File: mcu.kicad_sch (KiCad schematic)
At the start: 42 parts, among them J2 USB-C, J3 UART0, J4 I2C / Qwiic, J5 SPI, J6 WS2812, J7 Spare IO, J8 Rail break-out, Q4 AO3401A, Q5 MMBT3906, SW1 RESET, SW2 BOOT, U5 ESP32-S3-WROOM-1-N16R8, U6 TLV431A, U7 USBLC6-2SC6, U8 USBLC6-2SC6, U9 74AHCT1G125

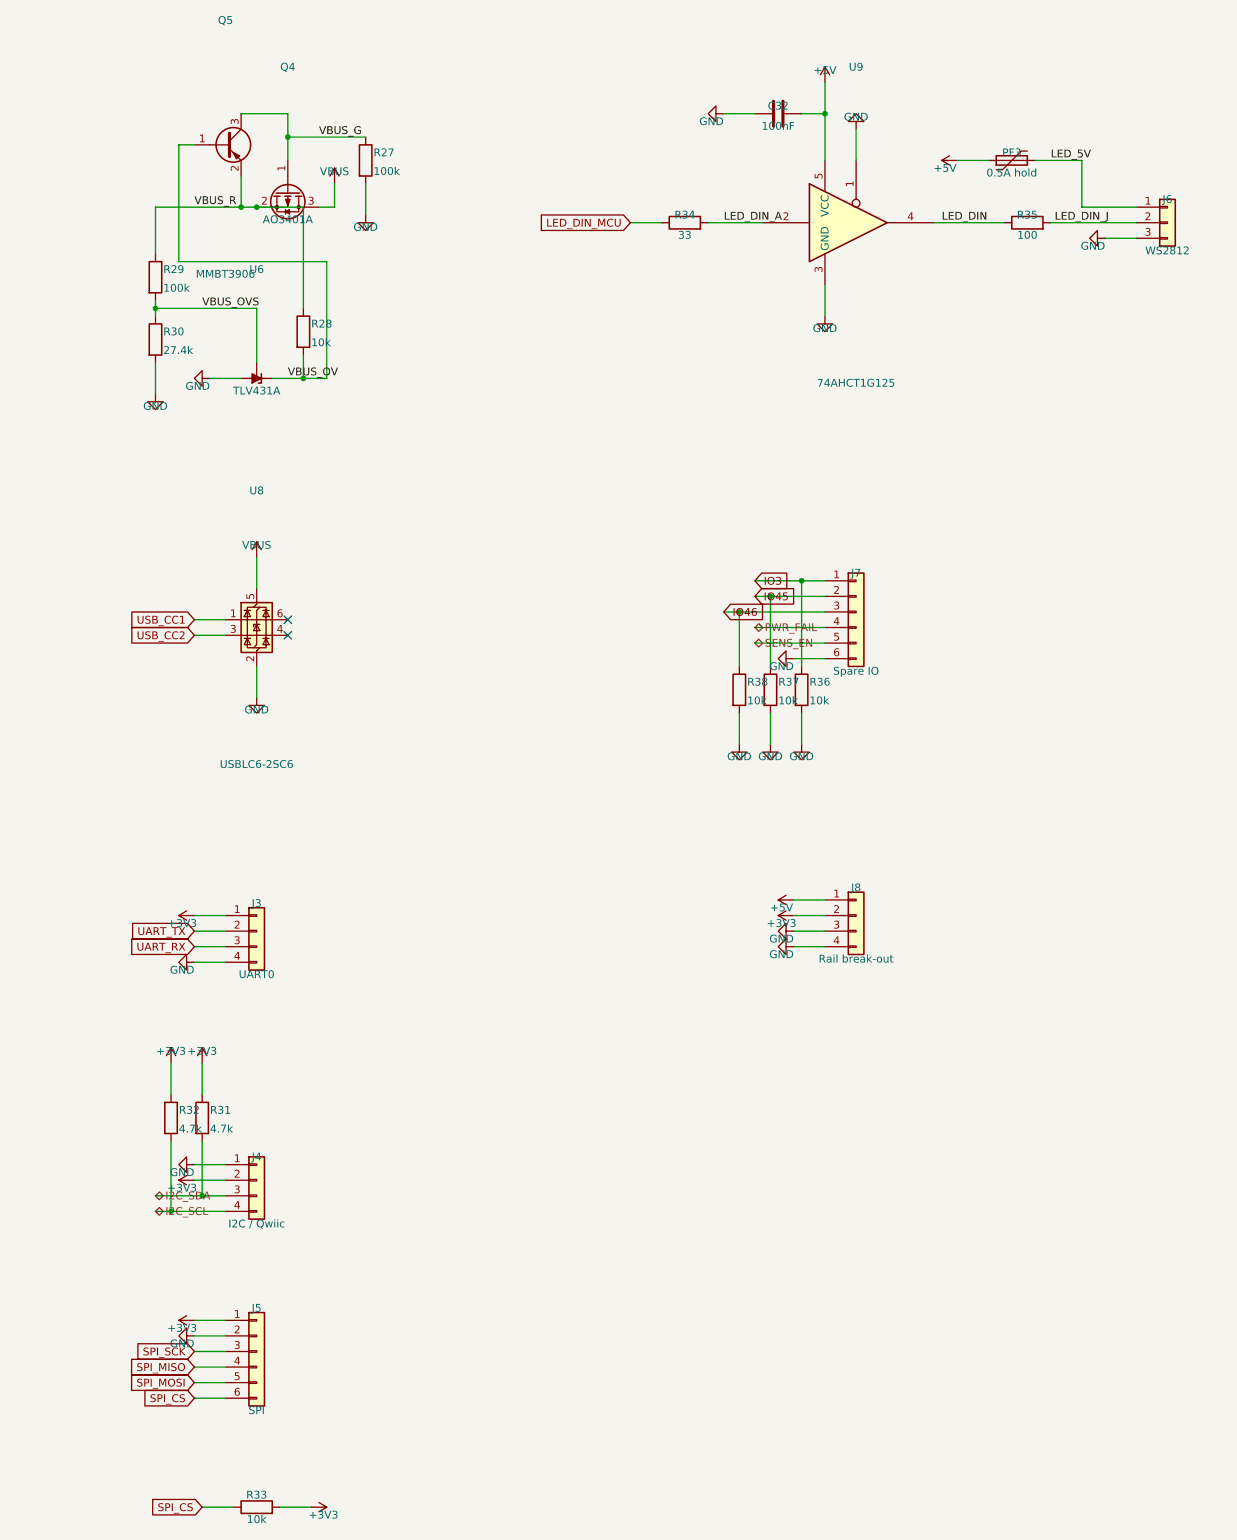
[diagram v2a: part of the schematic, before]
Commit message: Studies 9-11, post-route extraction, strap audit, readable labels, production BOM numbers
New tests, run against the final board:
- audit_routes.py: Dijkstra IR drop over the routed copper (worst 55 mV
  at rated current), SD/USB/CAN routed lengths (USB pair matched to
  1.1 mm), buck switch-node copper area. All clean.
- audit_straps.py: every ESP32-S3 strapping pin against what the netlist
  hangs on it; all five boot in their required state.
- simulate.py 9, stability: the LM5164 ripple-injection criterion across
  the input window. Found the ramp thin (10.6 mV) at a legitimate 8 V
  operating point -- ramp caps changed 3.3 nF -> 2.2 nF, now 15.8 mV+
  everywhere above crank voltages. Board rebuilt: 0 DRC, 0 unconnected,
  0 overlaps.
- simulate.py 10, CAN bus: TJA1051 through the choke and split
  termination into 5 m of terminated line -- 2.00 V dominant at the far
  end, no overshoot.
- simulate.py 11, budgets: enclosure thermal for the in-dash mount
  (sealed ABS is fine in the dash, would exceed the electrolytics' 105 C
  in an engine bay -- documented), fuse derating 69 %, I2C rise time vs
  Qwiic chains, WS2812 count, SD switch drop, connector contacts.
- tolerance MC gains the ride-through corner: 36 ms at caps -20 % /
  load +40 %, still covering a healthy-card flush.

Schematic readability, second pass: net-name labels moved onto short
vertical spurs clear of the circuits (deleting them outright renames
nets to Net-(R5-Pad2) and breaks name-based verification -- now in
gen/README.md), end-labels extend away from what they feed, and the
sensor-switch block redrawn at 1.5x pitch. Reversed-5V behaviour per
connector documented in the README.

BOM production pass: verified LCSC numbers added for the TVS families,
BAT54S, MM3Z zener and 2N7002s (21 numbered lines); the 39 blank lines
are JLC-auto-matched basic R/C; the 12 extended lines that must be
hand-matched in the order UI are listed in README 11. No guessed part
numbers.

gen/README.md gains the readab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
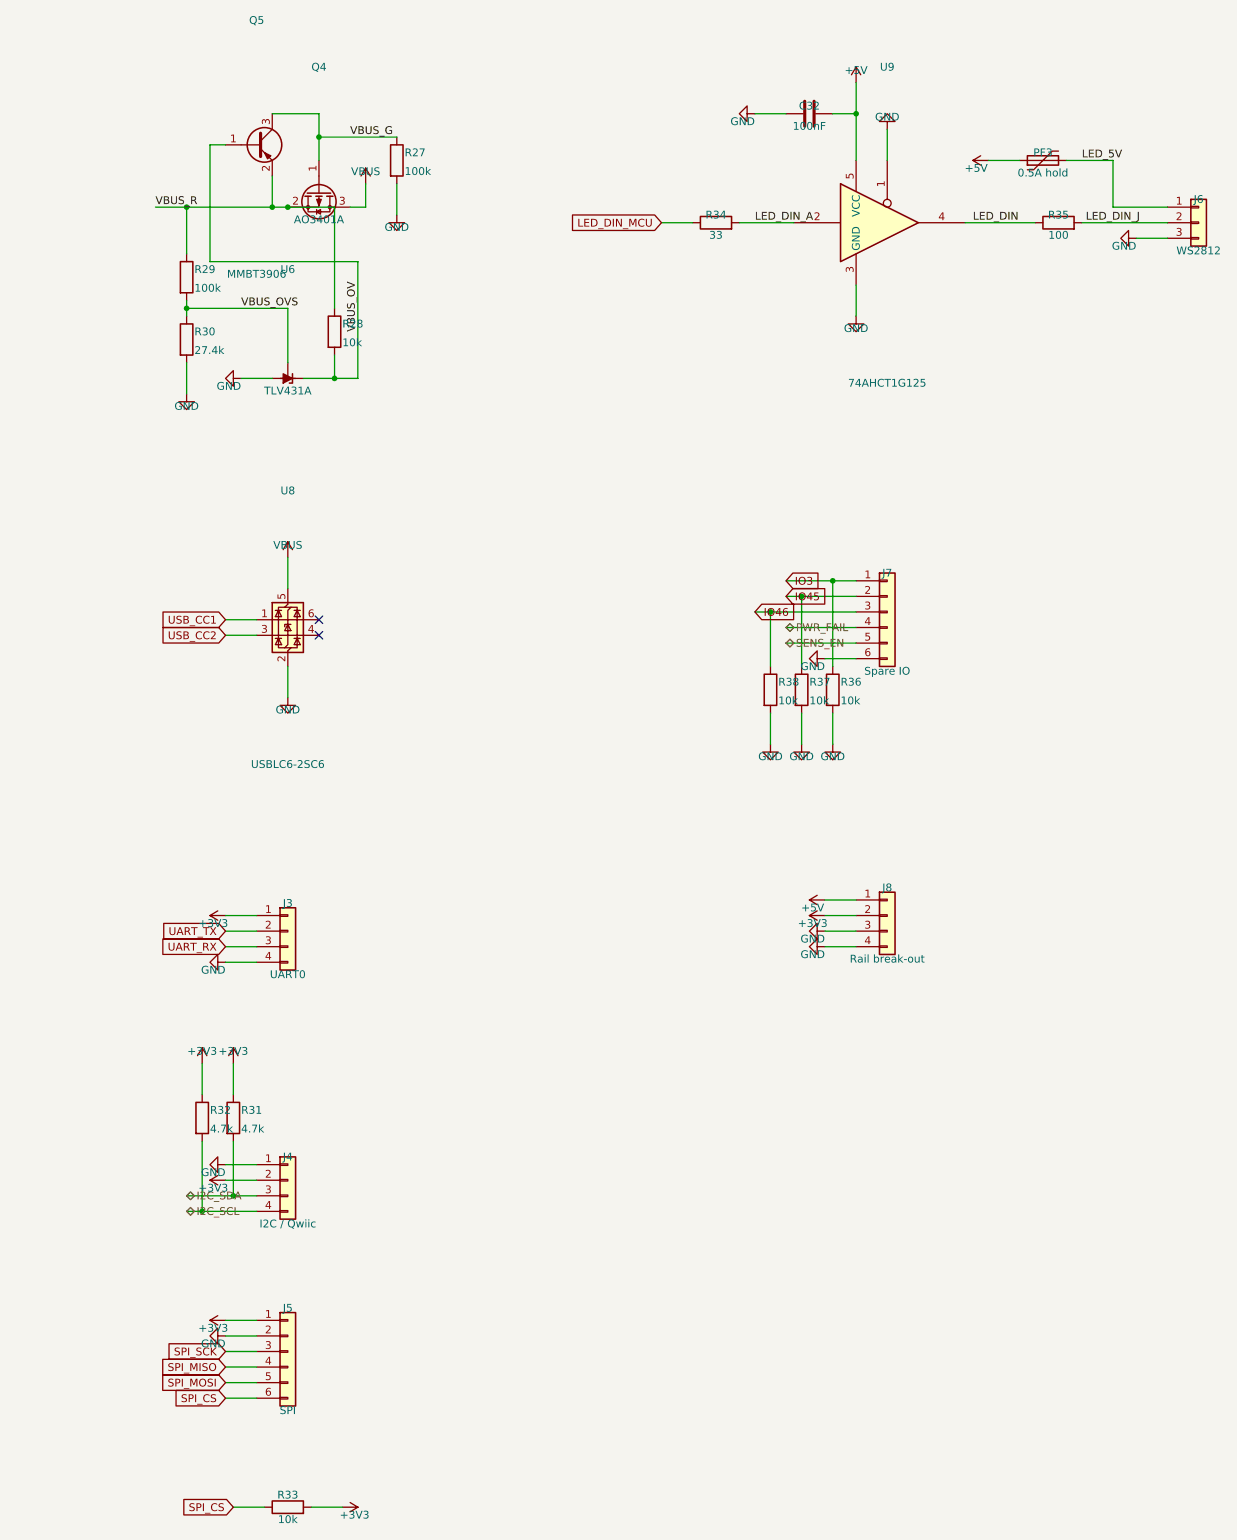
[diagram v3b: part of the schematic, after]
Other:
- moved on the sheet: C32, J3, J4, J5, J6, J7, J8, PF3, Q4, Q5, R27, R28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

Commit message: Verify every part number against the live catalogue; docs now self-check
Asked to make sure the part numbers will match real parts at order time, so
all 23 in fab/bom.csv were looked up one at a time against LCSC and the
JLCPCB parts library. Two were wrong, and one of them mattered.

  C8544 for Q5 "MMBT3906" resolves to an S9018 -- an NPN, from a different
  manufacturer. Q5 is the transistor that pulls the P-FET gate in the USB
  over-voltage cutoff, and it has to be a PNP. Ordering as it stood would
  have assembled the wrong polarity and left that protection silently
  inoperative. Now C84105, verified: ST(Semtech) MMBT3906, PNP, SOT-23.

  C7975 for U9 SN74AHCT1G125DBVR resolves to an LMV324IPWRG4, a quad op-amp
  in TSSOP-14, out of stock. The generator already knew -- it carried a
  comment saying so and left the field blank -- but the fix never reached
  README section 7, which still offered the number. Now C7484, verified.

L2's inductor picked up a verified number on the way past (C340243, the
22 uH sibling of L1's C340244), so the hand-match list at order time drops
from eleven lines to nine.

Also found while re-exporting: export_fab.py returned an empty set from
through_hole_refs() when pcbnew was missing, so running it under the system
Python produced fab files that looked perfect -- BOM and CPL still agreed,
designator counts still matched -- and quietly asked JLC to assemble all
eight hand-soldered connectors. It now re-execs under KiCad's Python, and
raises rather than degrading if that cannot be found. The files are back to
170 designators.

Documents brought in line with the artefacts: the Rev A title against a Rev
B board, 84 x 74 mm in three places on a board that is 84 x 100, stale
track/via/BOM/designator counts, and the ordering-day part-count split.

gen/audit_docs.py now recomputes ten of those numbers from the .kicad_pcb,
bom.csv and fab/ and diffs them against the prose. It immediately caught a
via count I had just got wrong by hand -- 3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
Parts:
- Q5: MPN onsemi MMBT3906 -> ST(Semtech) MMBT3906; Note Pulls the P-FET gate to its source on overvoltage -> Pulls the P-FET gate to its source on overvoltage. NOTE: th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
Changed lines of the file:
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@@
       (effects (font (size 1.27 1.27)) hide)
     )
-    (property "MPN" "onsemi MMBT3906" (at 251.46 49.02 0)
+    (property "MPN" "ST(Semtech) MMBT3906" (at 251.46 49.02 0)
       (effects (font (size 1.27 1.27)) hide)
     )
-    (property "Note" "Pulls the P-FET gate to its source on overvoltage" (at 251.46 49.02 0)
+    (property "Note" "Pulls the P-FET gate to its source on overvoltage. NOTE: this was C8544 until 2026-08-12, which is an S9018 -- an NPN, and not this part at all. Ordering it would have assembled the wrong polarity into the USB over-voltage cutoff and left the protection inoperative. Verified against the live catalogue: C84105 is an ST(Semtech) MMBT3906, PNP, SOT-23, 40 V" (at 251.46 49.02 0)
       (effects (font (size 1.27 1.27)) hide)
     )
